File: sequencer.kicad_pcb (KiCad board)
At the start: 2 copper layers, 171.4 x 106.7 mm, 435 parts, among them J1 PJ366ST, J10 PJ398SM, J11 PJ398SM, J12 PJ398SM, J13 PJ398SM, J14 PJ398SM, J15 PJ398SM, J16 PJ398SM, J17 PJ398SM, J18 PJ398SM, J19 PJ398SM, J2 PJ366ST, J20 PJ398SM, J21 PJ398SM, J22 PJ398SM, J23 PJ398SM, J24 PJ398SM, J25 PJ398SM, J26 PJ398SM, J3 PJ398SM, J4 PJ398SM, J5 PJ398SM, J6 PJ398SM, J7 PJ398SM, J8 PJ398SM, J9 PJ398SM, Q1 MMBT3904, Q2 MMBT3904, Q3 MMBT3904, Q4 MMBT3904, Q5 MMBT3904, SW1 TL1105, SW10 TL1105, SW11 TL1105, SW12 TL1105, SW13 TL1105, SW14 TL1105, SW15 TL1105, SW16 TL1105, SW17 TL1105, SW18 TL1105, SW19 EVQQ2, SW2 TL1105, SW20 TL1105, SW21 TL1105, SW22 TL1105, SW23 TL1105, SW24 TL1105, SW25 TL1105, SW26 TL1105, SW27 TL1105, SW28 TL1105, SW29 TL1105, SW3 TL1105, SW30 TL1105, SW31 TL1105, SW32 TL1105, SW33 TL1105, SW34 TL1105, SW35 TL1105, SW36 TL1105, SW37 TL1105, SW38 TL1105, SW39 TL1105, SW4 TL1105, SW5 TL1105, SW6 TL1105, SW7 TL1105, SW8 EVQQ2, SW9 TL1105, U1 VO0600T, U10 LM1117-3.3, U11 74HC165, U12 74HC595, U13 74HC595, U14 74HC595, U15 OPA4172, U16 R-78E5.0-1.0, U2 74LV1T34, U3 STMPS2151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

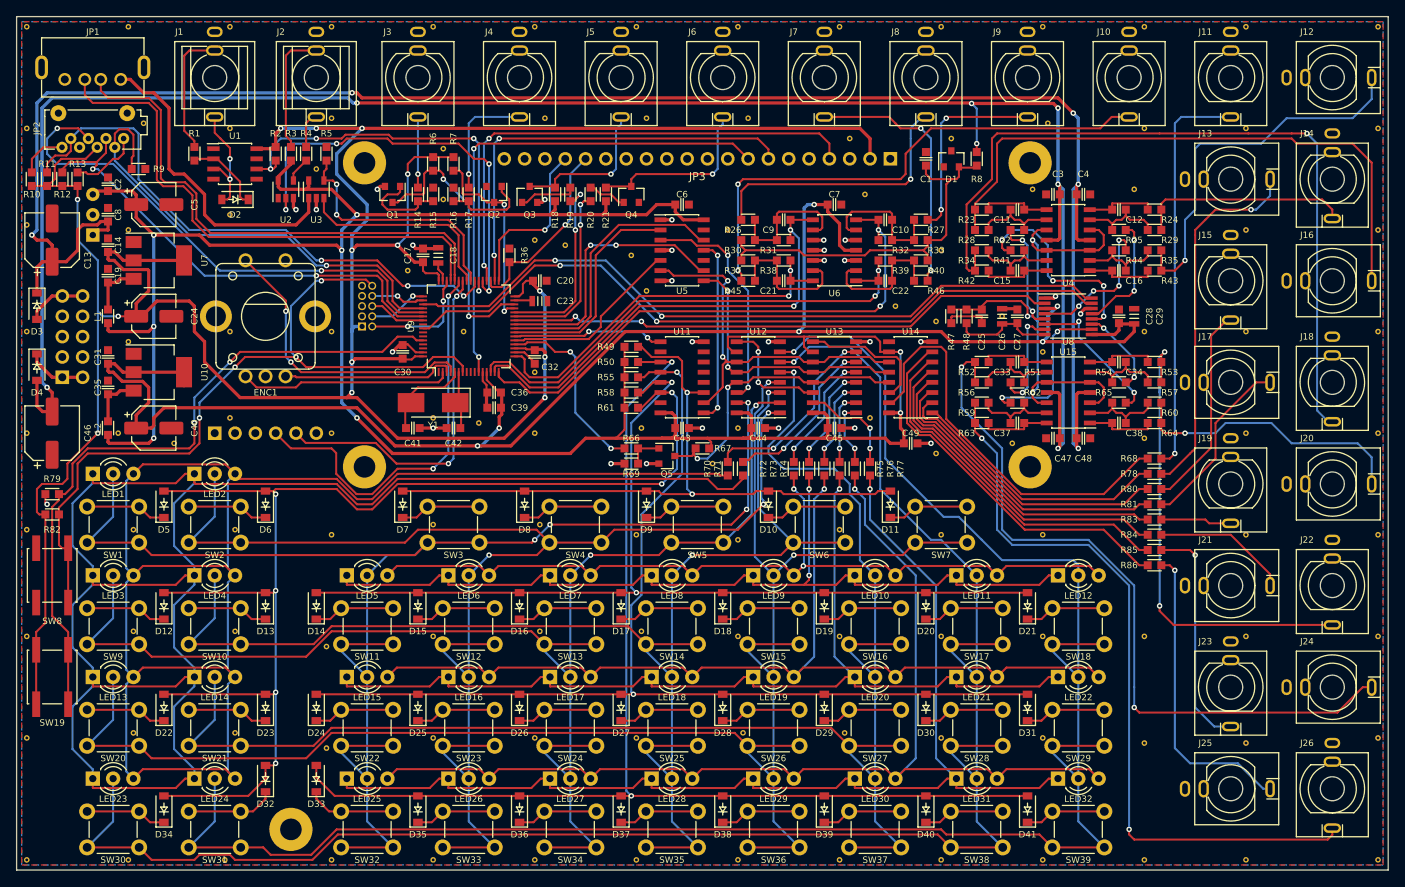
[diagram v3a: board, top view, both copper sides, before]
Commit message: add voltage supervisor, add leds to jacks, update footprints
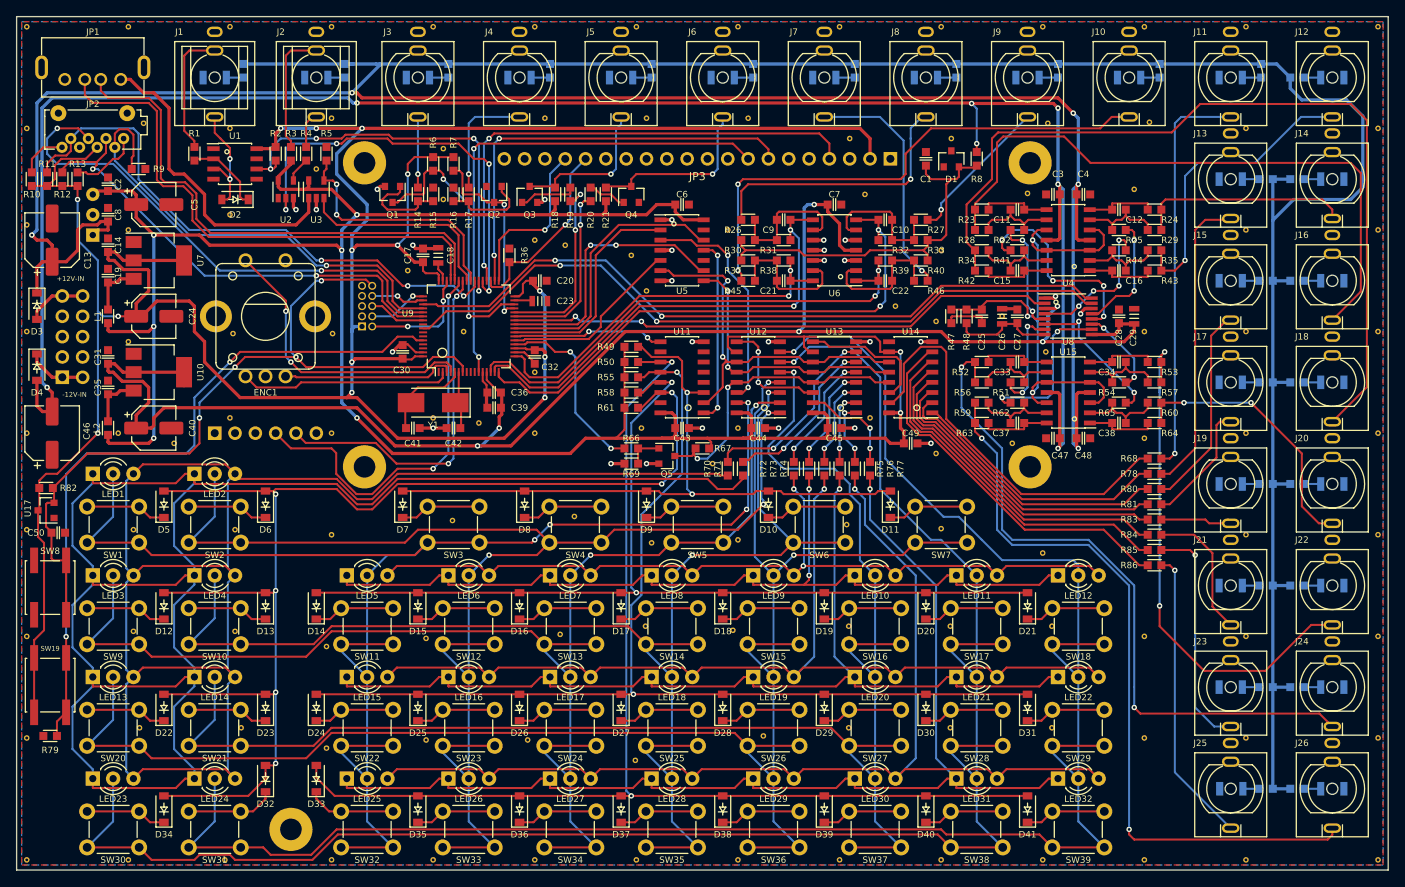
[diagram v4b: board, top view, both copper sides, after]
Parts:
- added C50: 100n, w_capacitor:C_0603, F.Cu at (82.0, 102.6)
- added D42: LED, w_capacitor:C_1206, B.Cu at (101.6, 45.7)
- added D43: LED, w_capacitor:C_1206, B.Cu at (114.3, 45.7)
- added D44: LED, w_capacitor:C_1206, B.Cu at (127.0, 45.7)
- added D45: LED, w_capacitor:C_1206, B.Cu at (165.1, 45.7)
- added D46: LED, w_capacitor:C_1206, B.Cu at (139.7, 45.7)
- added D47: LED, w_capacitor:C_1206, B.Cu at (177.8, 45.7)
- added D48: LED, w_capacitor:C_1206, B.Cu at (241.3, 83.8)
- added D49: LED, w_capacitor:C_1206, B.Cu at (152.4, 45.7)
- added D50: LED, w_capacitor:C_1206, B.Cu at (190.5, 45.7)
- added D51: LED, w_capacitor:C_1206, B.Cu at (228.6, 109.2)
- added D52: LED, w_capacitor:C_1206, B.Cu at (228.6, 96.5)
- added D53: LED, w_capacitor:C_1206, B.Cu at (228.6, 45.7)
- added D54: LED, w_capacitor:C_1206, B.Cu at (203.2, 45.7)
- added D55: LED, w_capacitor:C_1206, B.Cu at (241.3, 134.6)
- added D56: LED, w_capacitor:C_1206, B.Cu at (241.3, 96.5)
- added D57: LED, w_capacitor:C_1206, B.Cu at (241.3, 45.7)
- added D58: LED, w_capacitor:C_1206, B.Cu at (228.6, 71.1)
- added D59: LED, w_capacitor:C_1206, B.Cu at (215.9, 45.7)
- added D60: LED, w_capacitor:C_1206, B.Cu at (241.3, 121.9)
- added D61: LED, w_capacitor:C_1206, B.Cu at (241.3, 109.2)
- added D62: LED, w_capacitor:C_1206, B.Cu at (241.3, 71.1)
- added D63: LED, w_capacitor:C_1206, B.Cu at (228.6, 58.4)
- added D64: LED, w_capacitor:C_1206, B.Cu at (241.3, 58.4)
- added D65: LED, w_capacitor:C_1206, B.Cu at (228.6, 121.9)
- added D66: LED, w_capacitor:C_1206, B.Cu at (228.7, 134.6)
- added D67: LED, w_capacitor:C_1206, B.Cu at (228.6, 83.8)
- added R100: 1k, w_resistor:R_0603, B.Cu at (236.9, 134.6)
- added R101: 1k, w_resistor:R_0603, B.Cu at (236.9, 96.5)
- added R102: 1k, w_resistor:R_0603, B.Cu at (236.9, 45.7)
- added R103: 1k, w_resistor:R_0603, B.Cu at (233.0, 71.1)
- added R104: 1k, w_resistor:R_0603, B.Cu at (219.7, 44.9)
- added R105: 1k, w_resistor:R_0603, B.Cu at (236.9, 121.9)
- added R106: 1k, w_resistor:R_0603, B.Cu at (236.9, 109.2)
- added R107: 1k, w_resistor:R_0603, B.Cu at (236.9, 71.1)
- added R108: 1k, w_resistor:R_0603, B.Cu at (233.0, 58.4)
- added R109: 1k, w_resistor:R_0603, B.Cu at (236.9, 58.4)
- added R110: 1k, w_resistor:R_0603, B.Cu at (233.0, 121.9)
- added R111: 1k, w_resistor:R_0603, B.Cu at (233.0, 134.6)
- added R112: 1k, w_resistor:R_0603, B.Cu at (233.0, 83.8)
- added R87: 1k, w_resistor:R_0603, B.Cu at (105.2, 44.9)
- added R88: 1k, w_resistor:R_0603, B.Cu at (117.9, 44.9)
- added R89: 1k, w_resistor:R_0603, B.Cu at (130.8, 44.9)
- added R90: 1k, w_resistor:R_0603, B.Cu at (168.9, 44.9)
- added R91: 1k, w_resistor:R_0603, B.Cu at (143.5, 44.9)
- added R92: 1k, w_resistor:R_0603, B.Cu at (181.6, 44.9)
- added R93: 1k, w_resistor:R_0603, B.Cu at (236.9, 83.8)
- added R94: 1k, w_resistor:R_0603, B.Cu at (156.2, 44.9)
- added R95: 1k, w_resistor:R_0603, B.Cu at (194.3, 44.9)
- added R96: 1k, w_resistor:R_0603, B.Cu at (233.0, 109.2)
- added R97: 1k, w_resistor:R_0603, B.Cu at (233.0, 96.5)
- added R98: 1k, w_resistor:R_0603, B.Cu at (232.4, 44.9)
- added R99: 1k, w_resistor:R_0603, B.Cu at (207.0, 44.9)
- added U17: MIC803, Package_TO_SOT_SMD:SOT-23, F.Cu at (80.5, 99.8)
- J10, J11, J12, J13, J14, J15, J16, J17, J18, J19, J20, J21, J22, J23, J24, J25, J26, J3, J4, J5, J6, J7, J8, J9: footprint w_connector:PJ301M-12_Compact -> w_connector:jack_thonk
- U11, U12, U13, U14: footprint Package_SO:SOIC-16_3.9x9.9mm_P1.27mm -> w_ic:SOIC-16
- moved R79 30.2 mm to (81.0, 128.0)
- moved REF** 4.44 mm to (146.6, 100.6)
- moved R82 3.39 mm to (80.5, 97.0)
- moved REF** 2.80 mm to (154.2, 131.1)
- moved REF** 2.57 mm to (170.2, 128.0)
- moved REF** 2.57 mm to (144.8, 115.3)
- moved REF** 2.47 mm to (131.3, 101.1)
- moved REF** 2.29 mm to (205.1, 105.2)
- moved REF** 2.16 mm to (156.2, 103.9)
- moved REF** 1.71 mm to (206.2, 127.0)
- moved REF** 1.71 mm to (193.5, 127.0)
- moved REF** 1.71 mm to (206.2, 114.3)
- moved REF** 1.71 mm to (193.5, 114.3)
- moved REF** 1.71 mm to (180.8, 114.3)
- moved SW8 1.55 mm to (81.0, 109.5)
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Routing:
- net +12V: track 232.1 -> 495.0 mm
- net CV1: track 47.9 -> 38.3 mm
- net CV4: track 98.5 -> 107.8 mm, vias 1 -> 0
- net Net-(J13-Pad3): track 46.1 -> 37.9 mm, vias 1 -> 0
- net Net-(J17-Pad3): track 22.5 -> 15.3 mm
- net CV7: track 93.3 -> 87.3 mm
- net CV6: track 60.2 -> 66.1 mm
- net Net-(J9-Pad3): track 24.5 -> 18.7 mm, vias 2 -> 1
- net CV3: track 75.0 -> 79.6 mm
- net RESET: track 96.6 -> 101.2 mm
- net Net-(J7-Pad3): track 32.4 -> 30.0 mm, vias 2 -> 1
- net Net-(D59-Pad2): track 0.00 -> 2.36 mm
- net Net-(D50-Pad2): track 0.00 -> 2.36 mm
- net Net-(D49-Pad2): track 0.00 -> 2.36 mm
- net Net-(D47-Pad2): track 0.00 -> 2.36 mm
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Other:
- board text added: "+12V-IN"
- board text added: "-12V-IN"
- board text added: "cc-by-nc-sa Simon Kallweit 2020 board revision 1.1_dev"
- board text removed: "cc-by-nc-sa Simon Kallweit 2018 board revision 1.0"

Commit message: small changes
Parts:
- removed the REF** at (114.3, 57.1)
- added C51: ESD, w_capacitor:C_0603, F.Cu at (171.5, 50.6)
- added C52: ESD, w_capacitor:C_0603, F.Cu at (184.2, 50.6)
- added C53: ESD, w_capacitor:C_0603, F.Cu at (209.6, 47.5)
- added C54: ESD, w_capacitor:C_0603, F.Cu at (196.8, 50.6)
- added D68: 1N4148WS, Diode_SMD:D_SOD-123, F.Cu at (138.8, 60.3)
- added D69: 1N4148WS, Diode_SMD:D_SOD-123, F.Cu at (124.3, 56.1)
- added J27: Conn_01x03_Female, Connector_PinHeader_2.54mm:PinHeader_1x03_P2.54mm_Vertical, B.Cu at (121.0, 46.5)
- added REF**: VIA-0.6mm, w_via:VIA-0.7mm, F.Cu at (212.6, 95.0)
- added REF**: VIA-0.6mm, w_via:VIA-0.7mm, F.Cu at (208.3, 95.0)
- added REF**: VIA-0.6mm, w_via:VIA-0.7mm, F.Cu at (93.5, 58.5)
- added REF**: VIA-0.6mm, w_via:VIA-0.7mm, F.Cu at (111.2, 45.7)
- added REF**: VIA-0.6mm, w_via:VIA-0.7mm, F.Cu at (130.2, 61.5)
- C18, C23, C26, C29: footprint w_capacitor:C_0805 -> w_capacitor:C_0603
- U3: footprint Package_TO_SOT_SMD:SOT-23-5 -> Package_SO:TSSOP-8_4.4x3mm_P0.65mm
- moved R5 7.71 mm to (115.7, 63.0), turned to 270 degrees
- moved U3 5.10 mm to (110.5, 63.1), turned to 180 degrees
- moved REF** 4.77 mm to (107.5, 60.2)
- moved REF** 4.45 mm to (107.8, 50.8)
- moved REF** 1.28 mm to (198.8, 75.5)
- moved REF** 0.96 mm to (130.2, 60.0)
- moved U16 0.76 mm to (86.3, 62.1)
- moved Q3 0.63 mm to (141.6, 60.3)
- moved Q2 0.53 mm to (136.0, 60.3)
- moved U2 0.44 mm to (110.5, 59.2)
- turned D2 to 0 degrees
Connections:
- R100 pad 2: +12V -> LED_VDD
- R101 pad 2: +12V -> LED_VDD
- R102 pad 2: +12V -> LED_VDD
- R103 pad 2: +12V -> LED_VDD
- R104 pad 2: +12V -> LED_VDD
- R105 pad 2: +12V -> LED_VDD
- R106 pad 2: +12V -> LED_VDD
- R107 pad 2: +12V -> LED_VDD
- R108 pad 2: +12V -> LED_VDD
- R109 pad 2: +12V -> LED_VDD
- R110 pad 2: +12V -> LED_VDD
- R111 pad 2: +12V -> LED_VDD
- R112 pad 2: +12V -> LED_VDD
- R87 pad 2: +12V -> LED_VDD
- R88 pad 2: +12V -> LED_VDD
- R89 pad 2: +12V -> LED_VDD
- R90 pad 2: +12V -> LED_VDD
- R91 pad 2: +12V -> LED_VDD
- R92 pad 2: +12V -> LED_VDD
- R93 pad 2: +12V -> LED_VDD
- R94 pad 2: +12V -> LED_VDD
- R95 pad 2: +12V -> LED_VDD
- R96 pad 2: +12V -> LED_VDD
- R97 pad 2: +12V -> LED_VDD
- R98 pad 2: +12V -> LED_VDD
- R99 pad 2: +12V -> LED_VDD
- U3 pad 1: USB_5V -> GND
- U3 pad 2: GND -> +5V
- U3 pad 3: USB_PWR_FAULT -> +5V
- U3 pad 5: +5V -> USB_PWR_FAULT
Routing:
- net +12V: track 495.0 -> 231.0 mm
- net LED_VDD: track 0.00 -> 257.8 mm
- net Net-(C53-Pad2): track 66.1 -> 74.0 mm
- net USB_5V: track 39.4 -> 31.9 mm
- net USB_PWR_FAULT: track 25.9 -> 32.4 mm
- net MIDI_TX: track 53.9 -> 47.6 mm, vias 4 -> 2
- net Net-(C54-Pad2): track 18.7 -> 24.2 mm
- net Net-(C52-Pad2): track 34.2 -> 39.7 mm
- net Net-(C51-Pad2): track 30.0 -> 35.5 mm
- net +3V3: track 363.6 -> 359.0 mm, vias 14 -> 13
- net USB_PWR_EN: track 31.2 -> 27.1 mm, vias 2 -> 0
- net +3.3VA: track 213.3 -> 209.3 mm
- net +5V: track 310.3 -> 313.7 mm, vias 8 -> 9
- net MIDI_RX: track 52.7 -> 50.5 mm, vias 4 -> 2
- net GND: track 63.0 -> 65.2 mm, vias 27 -> 37
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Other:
- board text added: "LEDS"
- board text added: "cc-by-nc-sa Simon Kallweit 2020 board revision 1.3 by Diego Avila"
- board text removed: "cc-by-nc-sa Simon Kallweit 2020 board revision 1.1_dev"
